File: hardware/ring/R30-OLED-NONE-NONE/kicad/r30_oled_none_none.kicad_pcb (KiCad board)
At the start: 2 copper layers, 43 x 18 mm, 32 parts, among them J1 USB4215-class 16P TH stakes, Q1 SI2301 P-FET, Q2 2N7002 gate driver, SW1 5mm 200gf dome, U1 ESP32-C3-MINI-1-N4, U2 PAW3204DB-TJ3L, U3 TP4054, U4 RT9080-33GJ5

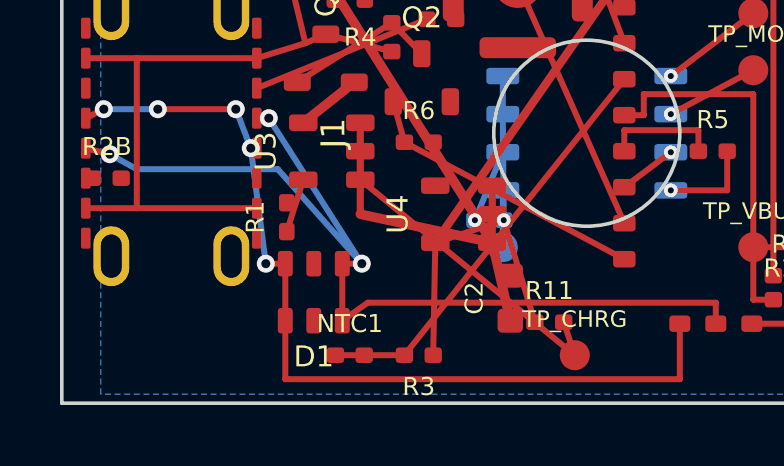
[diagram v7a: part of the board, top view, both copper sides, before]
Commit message: fix(r30): replace d1 rail clamp esd
Sensing mechanism: PAW3204 optical surface tracking with rail-less dual USB data ESD protection on the service connector.

Form factor and angle: R30 30-degree ring, OLED/NONE/NONE active lane; D1 changes from USBLC6 SOT-23-6 rail clamp to TPD2E2U06DCK-class SC-70/SOT-323 data shunt.

Intended use: accessibility-first BLE HID pointing first-board validation with offline USB service/debug retained.

BOM estimate: active R30 prototype remains about .30-.45, target about ; D1 stays in the same about /bin/zsh.03-/bin/zsh.10 ESD protection class.
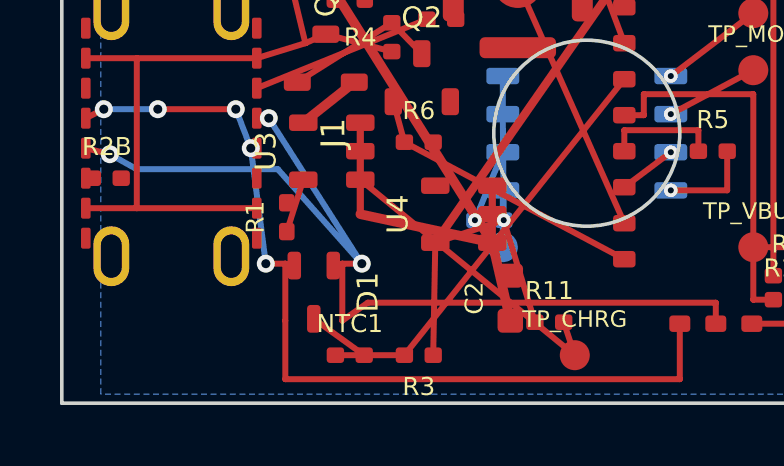
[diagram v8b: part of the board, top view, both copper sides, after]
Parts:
- D1: value USBLC6-2SC6-class -> TPD2E2U06DCK-class; footprint Package_TO_SOT_SMD:SOT-23-6 -> Package_TO_SOT_SMD:SOT-323_SC-70
- turned D1 to 270 degrees
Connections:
- D1 pad 2: GND -> USB_D-
- D1 pad 3: USB_D- -> GND
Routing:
- net GND: track 9.16 -> 11.2 mm
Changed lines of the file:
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@@
     (pad "5" smd roundrect (at -0.95 -0.95 90) (size 0.55 0.95) (layers "F.Cu" "F.Paste" "F.Mask") (roundrect_rratio 0.20) (net 5 "VREG_3V3") (pinfunction "VOUT") (pintype "power_out"))
   )
-  (footprint "Package_TO_SOT_SMD:SOT-23-6"
-    (layer "F.Cu")
-    (at 107.400 105.300 180)
-    (property "Reference" "D1" (at 0 -2.15 180) (layer "F.SilkS") (effects (font (size 0.7 0.7) (thickness 0.1))))
-    (property "Value" "USBLC6-2SC6-class" (at 0 2.15 180) (layer "F.Fab") (effects (font (size 0.7 0.7) (thickness 0.1))))
-    (property "mfg_part_num" "USBLC6-2SC6" (at 0 0 180) (layer "F.Fab") hide (effects (font (size 0.7 0.7))))
-    (property "manufacturer" "STMicroelectronics" (at 0 0 180) (layer "F.Fab") hide (effects (font (size 0.7 0.7))))
-    (property "lcsc" "" (at 0 0 180) (layer "F.Fab") hide (effects (font (size 0.7 0.7))))
-    (fp_rect (start -1.45 -1.05) (end 1.45 1.05) (stroke (width 0.10) (type solid)) (fill none) (layer "F.Fab"))
-    (pad "1" smd roundrect (at -0.95 0.95 180) (size 0.50 0.85) (layers "F.Cu" "F.Paste" "F.Mask") (roundrect_rratio 0.20) (net 16 "USB_D+") (pinfunction "I/O1") (pintype "passive"))
-    (pad "2" smd roundrect (at 0 0.95 180) (size 0.50 0.85) (layers "F.Cu" "F.Paste" "F.Mask") (roundrect_rratio 0.20) (net 1 "GND") (pinfunction "GND") (pintype "power_in"))
-    (pad "3" smd roundrect (at 0.95 0.95 180) (size 0.50 0.85) (layers "F.Cu" "F.Paste" "F.Mask") (roundrect_rratio 0.20) (net 17 "USB_D-") (pinfunction "I/O2") (pintype "passive"))
-    (pad "4" smd roundrect (at 0.95 -0.95 180) (size 0.50 0.85) (layers "F.Cu" "F.Paste" "F.Mask") (roundrect_rratio 0.20) (net 17 "USB_D-") (pinfunction "I/O2") (pintype "passive"))
-    (pad "5" smd roundrect (at 0 -0.95 180) (size 0.50 0.85) (layers "F.Cu" "F.Paste" "F.Mask") (roundrect_rratio 0.20) (net 2 "VBUS_5V") (pinfunction "VBUS") (pintype "power_in"))
-    (pad "6" smd roundrect (at -0.95 -0.95 180) (size 0.50 0.85) (layers "F.Cu" "F.Paste" "F.Mask") (roundrect_rratio 0.20) (net 16 "USB_D+") (pinfunction "I/O1") (pintype "passive"))
+  (footprint "Package_TO_SOT_SMD:SOT-323_SC-70"
+    (layer "F.Cu")
+    (at 107.400 105.300 270)
+    (descr "TPD2E2U06-class rail-less dual USB data ESD in SC-70/SOT-323")
+    (tags "USB ESD rail-less dual data SC-70 SOT-323")
+    (property "Reference" "D1" (at 0 -1.80 270) (layer "F.SilkS") (effects (font (size 0.7 0.7) (thickness 0.1))))
+    (property "Value" "TPD2E2U06DCK-class" (at 0 1.80 270) (layer "F.Fab") (effects (font (size 0.7 0.7) (thickness 0.1))))
+    (property "mfg_part_num" "TPD2E2U06DCK" (at 0 0 270) (layer "F.Fab") hide (effects (font (size 0.7 0.7))))
+    (property "manufacturer" "Texas Instruments" (at 0 0 270) (layer "F.Fab") hide (effects (font (size 0.7 0.7))))
+    (property "lcsc" "" (at 0 0 270) (layer "F.Fab") hide (effects (font (size 0.7 0.7))))
+    (fp_rect (start -1.05 -0.85) (end 1.05 0.85) (stroke (width 0.10) (type solid)) (fill none) (layer "F.Fab"))
+    (pad "1" smd roundrect (at -0.8875 -0.65 270) (size 0.925 0.45) (layers "F.Cu" "F.Paste" "F.Mask") (roundrect_rratio 0.25) (net 16 "USB_D+") (pinfunction "IO1") (pintype "passive"))
+    (pad "2" smd roundrect (at -0.8875 0.65 270) (size 0.925 0.45) (layers "F.Cu" "F.Paste" "F.Mask") (roundrect_rratio 0.25) (net 17 "USB_D-") (pinfunction "IO2") (pintype "passive"))
+    (pad "3" smd roundrect (at 0.8875 0 270) (size 0.925 0.45) (layers "F.Cu" "F.Paste" "F.Mask") (roundrect_rratio 0.25) (net 1 "GND") (pinfunction "GND") (pintype "power_in"))
   )
   (footprint "PowerFinger_Ring:Snap_Dome_5mm_TwoPad_Serviceable"
@@
   (segment (start 109.000 104.350) (end 108.350 104.350) (width 0.20) (layer "F.Cu") (net 16))
   (segment (start 108.350 104.350) (end 108.350 106.250) (width 0.20) (layer "F.Cu") (net 16))
+  (segment (start 108.350 104.350) (end 108.050 104.412) (width 0.20) (layer "F.Cu") (net 16))
   (segment (start 108.350 106.250) (end 109.200 105.650) (width 0.20) (layer "F.Cu") (net 16))
   (segment (start 109.200 105.650) (end 120.800 105.650) (width 0.20) (layer "F.Cu") (net 16))
@@
   (segment (start 105.300 100.500) (end 105.800 104.350) (width 0.20) (layer "B.Cu") (net 17))
   (segment (start 105.800 104.350) (end 106.450 104.350) (width 0.20) (layer "F.Cu") (net 17))
+  (segment (start 106.450 104.350) (end 106.750 104.412) (width 0.20) (layer "F.Cu") (net 17))
   (segment (start 106.450 104.350) (end 106.450 106.250) (width 0.20) (layer "F.Cu") (net 17))
   (segment (start 106.450 106.250) (end 106.450 108.200) (width 0.20) (layer "F.Cu") (net 17))
@@
   (segment (start 122.050 105.550) (end 122.050 103.800) (width 0.20) (layer "F.Cu") (net 22))
   (segment (start 113.700 101.905) (end 113.700 103.800) (width 0.20) (layer "B.Cu") (net 23))
+  (segment (start 107.400 106.188) (end 109.080 107.400) (width 0.20) (layer "F.Cu") (net 1))
   (via (at 113.730 102.900) (size 0.46) (drill 0.20) (layers "F.Cu" "B.Cu") (net 5))
   (via (at 112.770 102.900) (size 0.46) (drill 0.20) (layers "F.Cu" "B.Cu") (net 1))
